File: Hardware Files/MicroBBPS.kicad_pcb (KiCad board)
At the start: 2 copper layers, 54 x 100 mm, 24 parts, among them J1 Conn_01x06, J2 USB_B_Micro, J3 Conn_02x03_Counter_Clockwise, J4 Conn_02x03_Counter_Clockwise, J5 Conn_01x02, J8 3PoleHeaderSwitch, J9 3PoleHeaderSwitch, U1 NCP1117ST50T3G, U3 NCP1117ST33T3G

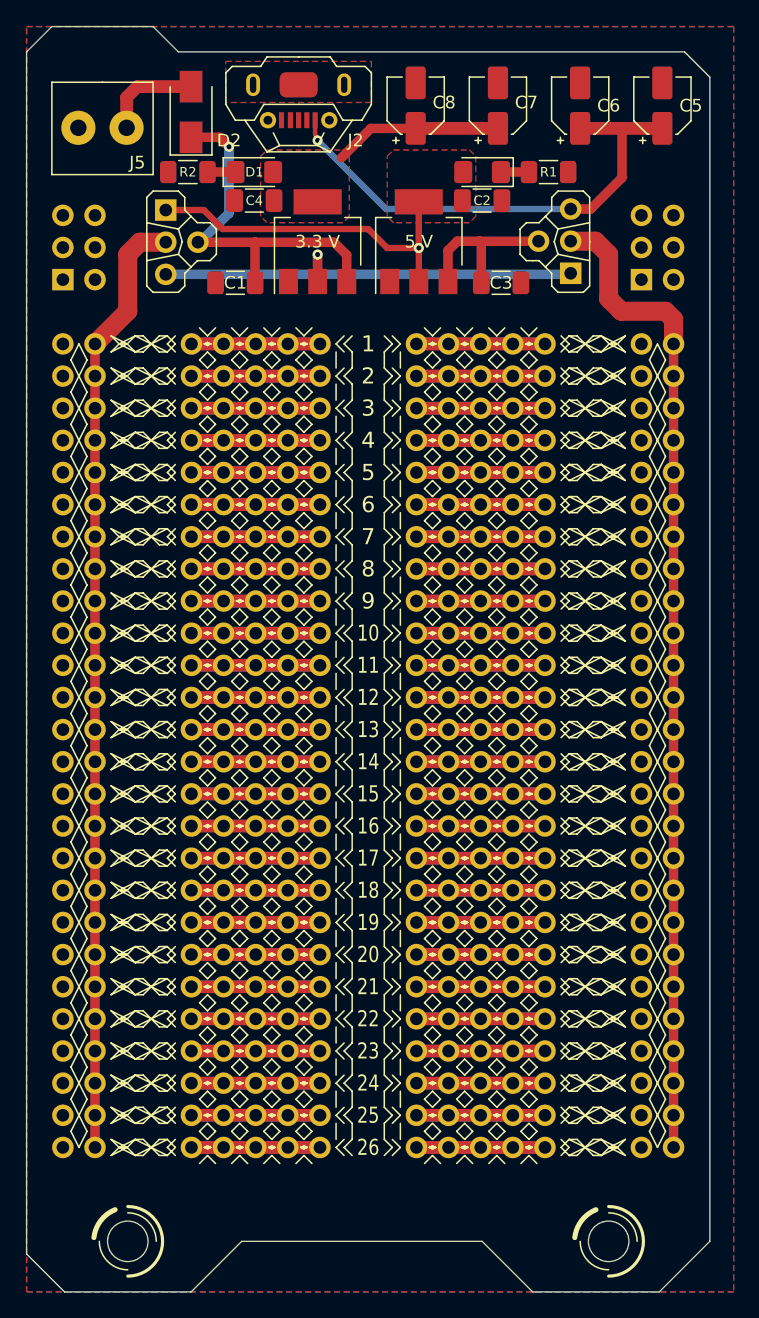
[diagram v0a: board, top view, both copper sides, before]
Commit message: Update Board shape and fix some routing
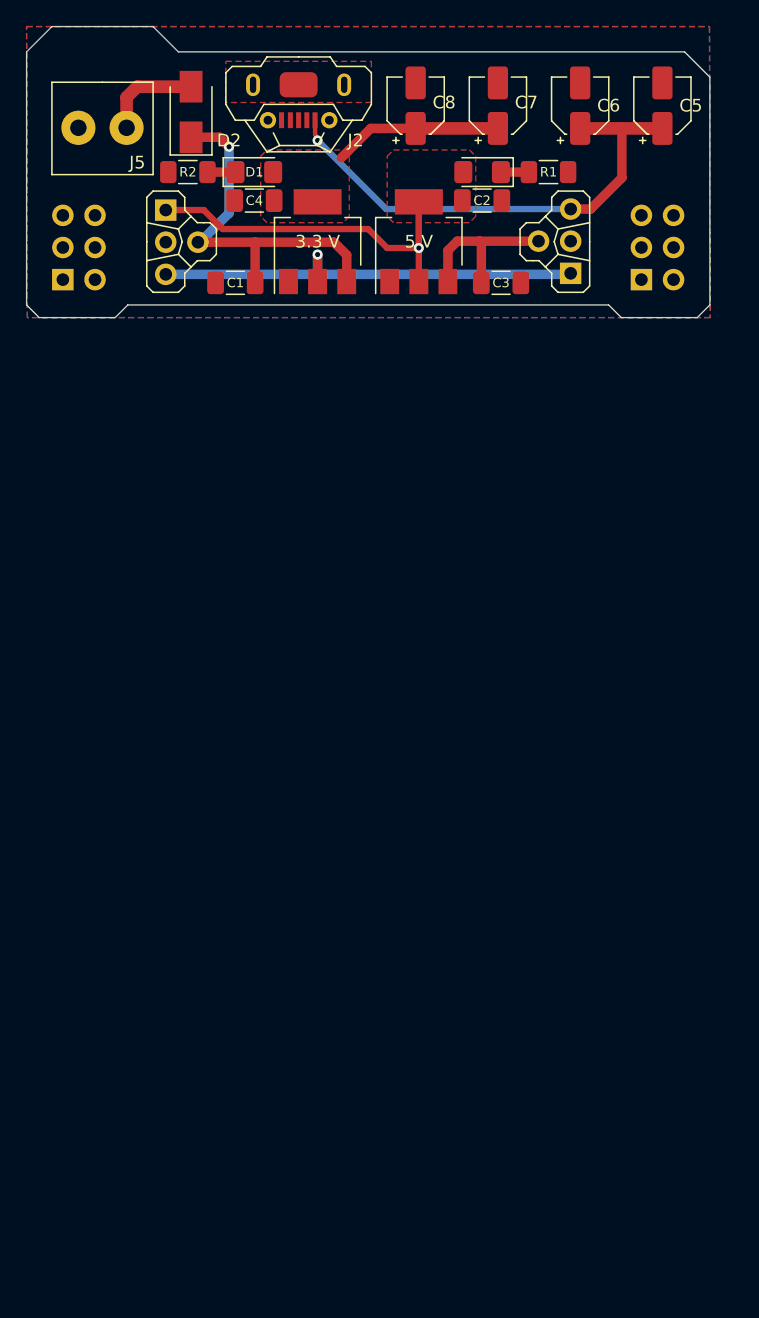
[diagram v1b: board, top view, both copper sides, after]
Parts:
- removed J1: Conn_01x06, MicroBBPS:Breadboard_Row_25
- removed REF** (x2): MountingHole_3.2mm_M3_ISO7380, MountingHole:MountingHole_3.2mm_M3_ISO7380
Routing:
- net /VoutRight: track 78.2 -> 0.00 mm
- net /VoutLeft: track 75.1 -> 0.00 mm
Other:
- board size 54 x 100 mm -> 54 x 23 mm

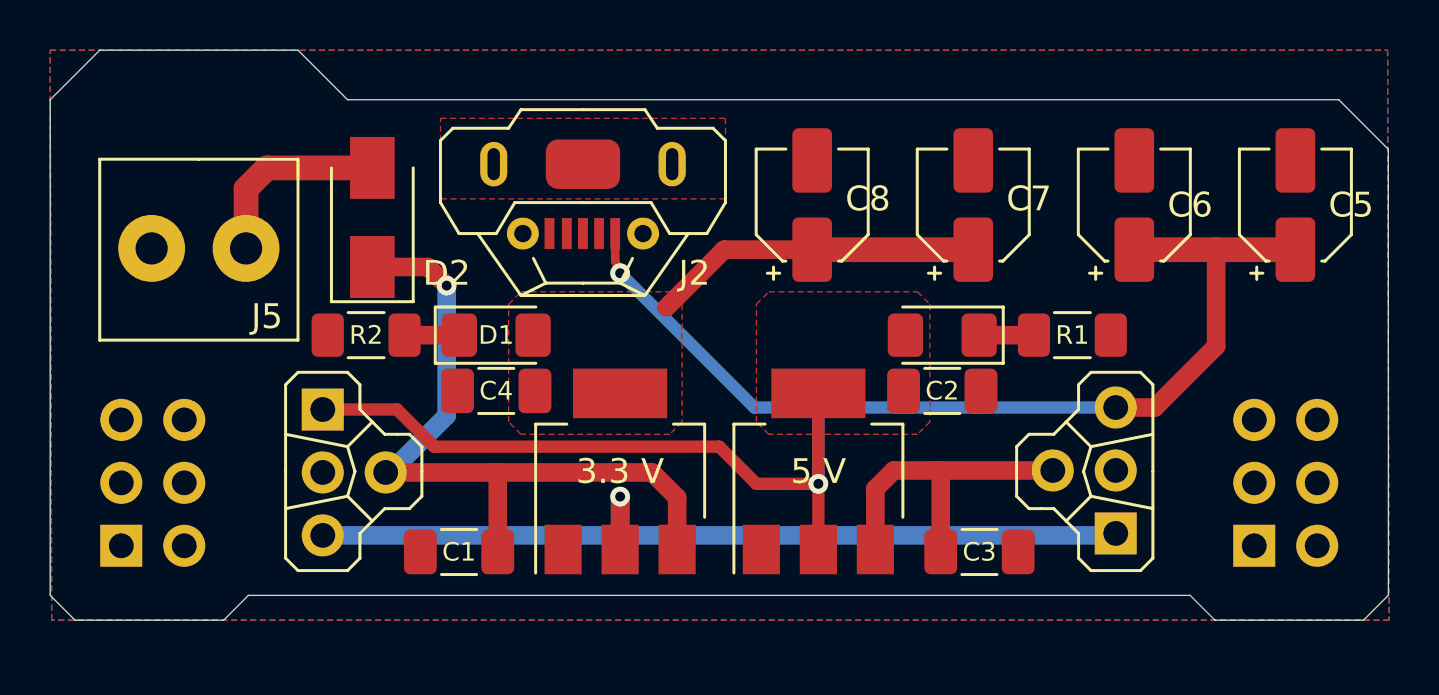
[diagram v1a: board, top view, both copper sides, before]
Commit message: Finalize routing and board shape
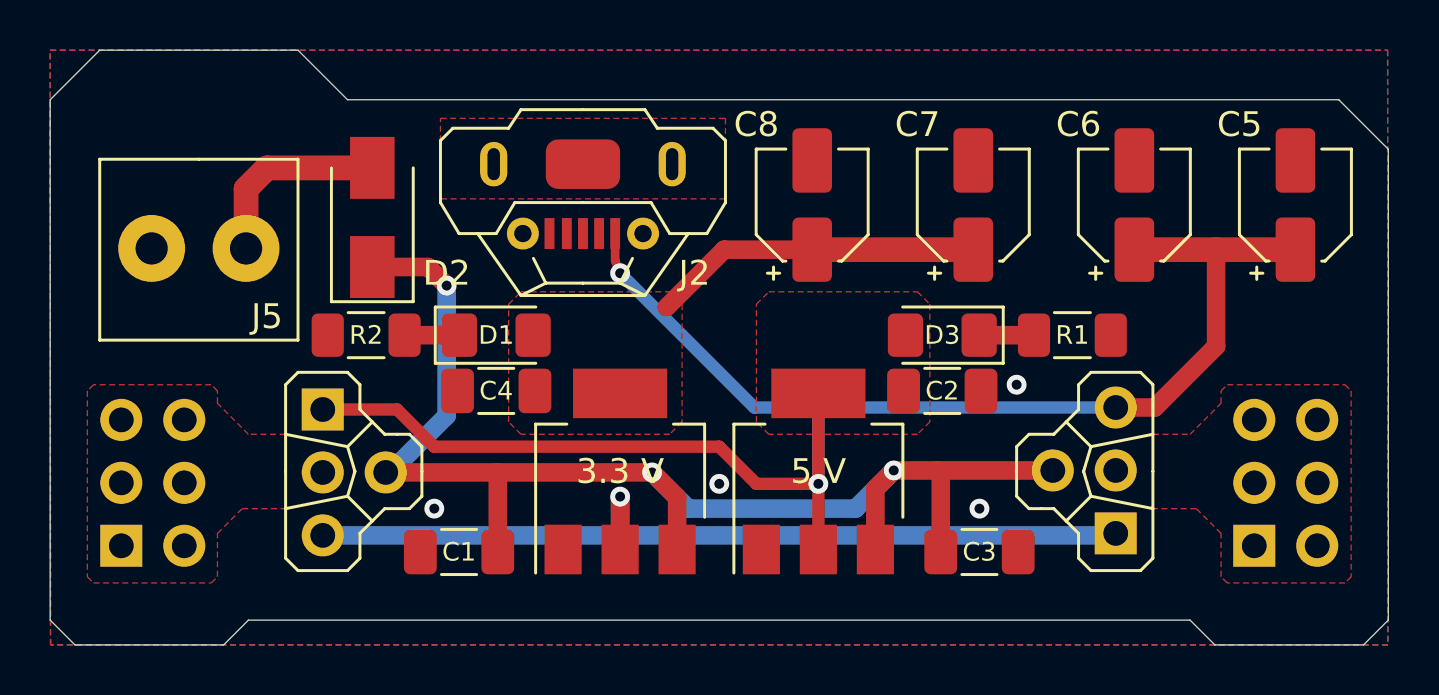
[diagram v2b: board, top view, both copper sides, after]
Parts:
- J3, J4: value Conn_02x03_Counter_Clockwise -> Conn_02x03
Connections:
- J3 pad 1: Net-(J3-Pad1) -> GND
- J3 pad 2: Net-(J3-Pad2) -> /VoutLeft
- J3 pad 3: Net-(J3-Pad3) -> GND
- J3 pad 4: Net-(J3-Pad4) -> /VoutLeft
- J3 pad 5: Net-(J3-Pad5) -> GND
- J3 pad 6: Net-(J3-Pad6) -> /VoutLeft
- J4 pad 1: Net-(J4-Pad1) -> GND
- J4 pad 2: Net-(J4-Pad2) -> /VoutRight
- J4 pad 3: Net-(J4-Pad3) -> GND
- J4 pad 4: Net-(J4-Pad4) -> /VoutRight
- J4 pad 5: Net-(J4-Pad5) -> GND
- J4 pad 6: Net-(J4-Pad6) -> /VoutRight
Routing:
- net VS: track 42.7 -> 53.7 mm, vias 1 -> 3
- net GND: vias 0 -> 4
- added copper zone on F.Cu, net /VoutLeft
- added copper zone on F.Cu, net /VoutRight
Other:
- board size 54 x 23 mm -> 54 x 24 mm

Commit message: Begin artwork
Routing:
- net (no net): track 0.00 -> 6.83 mm
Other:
- outline, holes or cut-outs redrawn
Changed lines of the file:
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@@
   (general
     (thickness 1.6)
-    (drawings 32)
-    (tracks 64)
+    (drawings 38)
+    (tracks 70)
     (zones 0)
     (modules 21)
@@
     (38 B.Mask user hide)
     (39 F.Mask user hide)
-    (40 Dwgs.User user)
+    (40 Dwgs.User user hide)
     (41 Cmts.User user hide)
     (42 Eco1.User user)
@@
   )
   (setup
-    (last_trace_width 0.75)
+    (last_trace_width 0.2)
     (user_trace_width 0.2)
     (user_trace_width 0.25)
@@
     )
   )
+  (gr_line (start 0 0) (end 1 0) (layer B.SilkS) (width 0.2))
+  (gr_line (start 0 0) (end 0 1) (layer B.SilkS) (width 0.2))
+  (gr_line (start 0 0) (end 1 0) (layer F.SilkS) (width 0.2))
+  (gr_line (start 0 0) (end 0 1) (layer F.SilkS) (width 0.2))
+  (gr_line (start 1 0) (end 0 0) (layer Edge.Cuts) (width 0.2))
+  (gr_line (start 0 0) (end 0 1) (layer Edge.Cuts) (width 0.2))
   (dimension 54 (width 0.15) (layer Dwgs.User)
     (gr_text "54.000 mm" (at 27 29.299999) (layer Dwgs.User)
@@
   (gr_poly (pts (xy 210.631 108.514) (xy 210.25 108.895) (xy 209.869 108.514) (xy 210.25 108.133)) (layer F.Mask) (width 0.1))
   (gr_poly (pts (xy 211.266 107.879) (xy 210.885 108.26) (xy 210.504 107.879) (xy 210.885 107.498)) (layer F.Mask) (width 0.1))
+  (segment (start 0 0) (end 0 1) (width 0.2) (layer F.Cu) (net 0))
+  (segment (start 0 1) (end 1 0) (width 0.2) (layer F.Cu) (net 0))
+  (segment (start 1 0) (end 0 0) (width 0.2) (layer F.Cu) (net 0))
+  (segment (start 0 0) (end 0 1) (width 0.2) (layer B.Cu) (net 0))
+  (segment (start 0 1) (end 1 0) (width 0.2) (layer B.Cu) (net 0))
+  (segment (start 1 0) (end 0 0) (width 0.2) (layer B.Cu) (net 0))
   (via (at 15.5 18.5) (size 0.8) (drill 0.4) (layers F.Cu B.Cu) (net 1))
   (via (at 27 17.5) (size 0.8) (drill 0.4) (layers F.Cu B.Cu) (net 1))

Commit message: Finalize artwork, add missing files
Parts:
- added G***: LOGO, MicroBBPS:artwork-bottom, B.Cu at (27.0, 12.0)
- added G***: LOGO, MicroBBPS:artwork-top, F.Cu at (27.0, 12.0)
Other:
- outline, holes or cut-outs redrawn

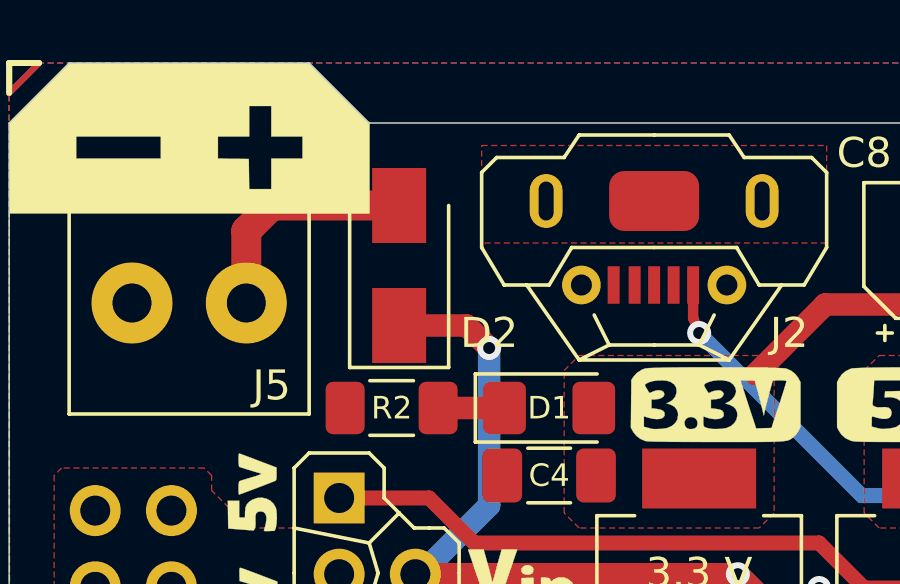
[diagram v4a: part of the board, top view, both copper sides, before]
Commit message: fab file plotting
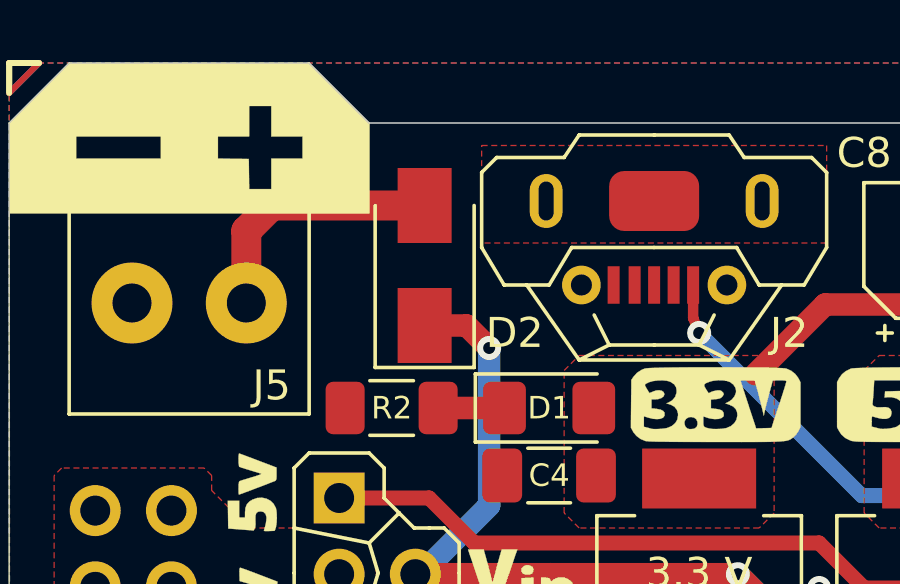
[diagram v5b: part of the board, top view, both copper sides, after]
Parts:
- moved D2 0.85 mm to (13.8, 6.75)
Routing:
- net VS: track 53.7 -> 52.9 mm
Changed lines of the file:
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@@
   )
   (module Diode_SMD:D_SMA (layer F.Cu)
-    (at 13 6.75 90)
+    (at 13.85 6.75 90)
     (descr "Diode SMA (DO-214AC)")
     (tags "Diode SMA (DO-214AC)")
@@
   (segment (start 35.79 16.96) (end 34.04 16.96) (width 0.75) (layer F.Cu) (net 2))
   (segment (start 40.46 16.96) (end 35.79 16.96) (width 0.75) (layer F.Cu) (net 2))
-  (segment (start 13 8.75) (end 15.25 8.75) (width 0.75) (layer F.Cu) (net 2))
   (via (at 16 9.5) (size 0.8) (drill 0.4) (layers F.Cu B.Cu) (net 2))
-  (segment (start 15.25 8.75) (end 16 9.5) (width 0.75) (layer F.Cu) (net 2))
   (segment (start 16 9.5) (end 16 14.75) (width 0.75) (layer B.Cu) (net 2))
   (segment (start 13.71 17.04) (end 13.54 17.04) (width 0.75) (layer B.Cu) (net 2))
@@
   (segment (start 25.75 18.5) (end 24.29 17.04) (width 0.75) (layer B.Cu) (net 2))
   (segment (start 32.5 18.5) (end 25.75 18.5) (width 0.75) (layer B.Cu) (net 2))
+  (segment (start 15.25 8.75) (end 16 9.5) (width 0.75) (layer F.Cu) (net 2))
+  (segment (start 13.85 8.75) (end 15.25 8.75) (width 0.75) (layer F.Cu) (net 2))
   (segment (start 43 14.42) (end 44.58 14.42) (width 0.75) (layer F.Cu) (net 3))
   (segment (start 47.05 11.95) (end 47.05 8.05) (width 0.75) (layer F.Cu) (net 3))
